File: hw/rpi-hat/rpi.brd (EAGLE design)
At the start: 65 x 56.5 mm, 30 parts, among them U1 BSS138, U2 BSS138, U3 BSS138

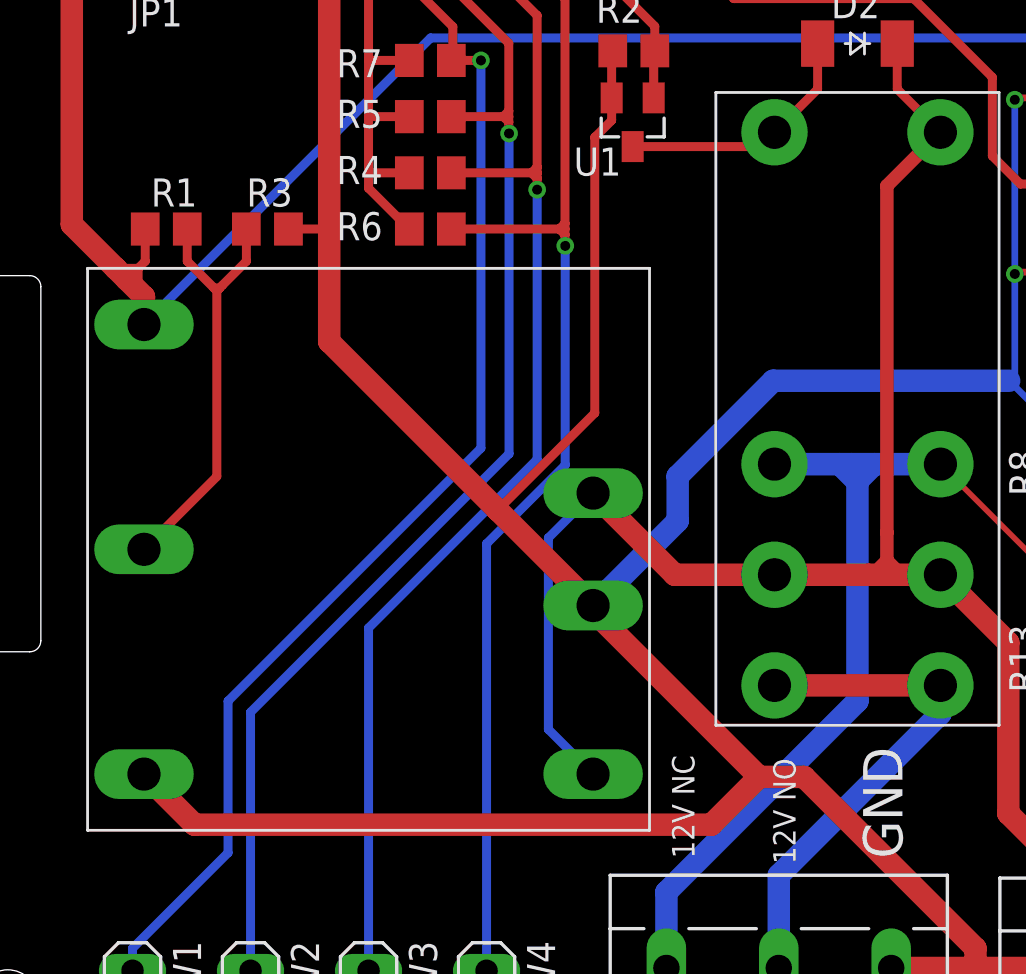
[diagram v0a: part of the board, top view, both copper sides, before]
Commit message: rpi hat: fix a few traces being to close to vias
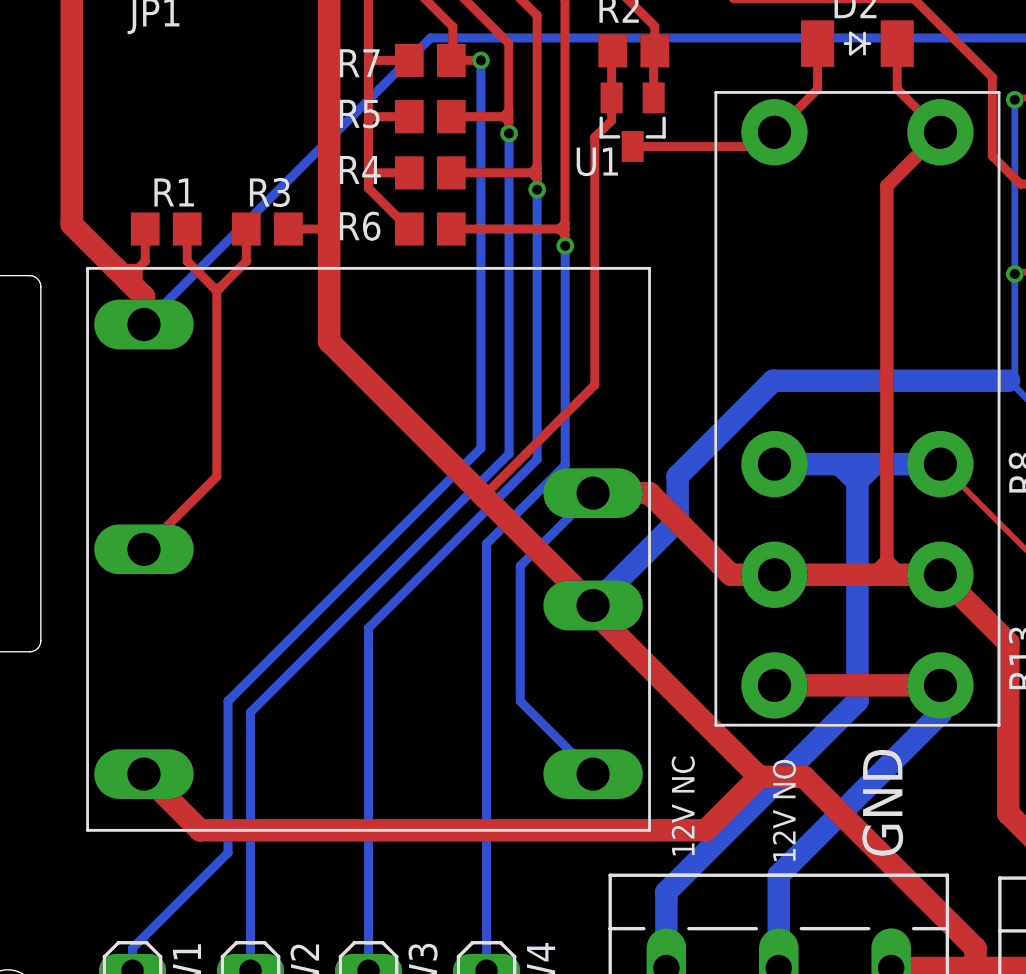
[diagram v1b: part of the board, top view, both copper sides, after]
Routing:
- net +12V: track 81.5 -> 82.5 mm
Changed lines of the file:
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@@
 <wire x1="30.85" y1="46.662" x2="30.8" y2="46.612" width="0.4064" layer="1"/>
 <wire x1="30.8" y1="46.612" x2="30.8" y2="44.534" width="0.4064" layer="1"/>
-<wire x1="9.662" y1="13.97" x2="11.948" y2="11.684" width="1.016" layer="1"/>
-<wire x1="11.948" y1="11.684" x2="35.306" y2="11.684" width="1.016" layer="1"/>
+<wire x1="9.662" y1="13.97" x2="12.202" y2="11.43" width="1.016" layer="1"/>
+<wire x1="12.202" y1="11.43" x2="35.052" y2="11.43" width="1.016" layer="1"/>
 <contactref element="SW4" pad="2"/>
 <contactref element="SW1" pad="2"/>
@@
 <contactref element="SW3" pad="2"/>
 <wire x1="18.034" y1="33.518" x2="18.034" y2="38.608" width="1.016" layer="1"/>
-<wire x1="29.962" y1="21.59" x2="25.649" y2="25.903" width="1.016" layer="1"/>
-<wire x1="25.649" y1="25.903" x2="18.034" y2="33.518" width="1.016" layer="1"/>
+<wire x1="29.962" y1="21.59" x2="25.014" y2="26.538" width="1.016" layer="1"/>
+<wire x1="25.014" y1="26.538" x2="18.034" y2="33.518" width="1.016" layer="1"/>
 <wire x1="16.19" y1="38.608" x2="18.034" y2="38.608" width="0.4064" layer="1"/>
 <wire x1="9.144" y1="2.54" x2="14.478" y2="2.54" width="0.4064" layer="1"/>
@@
 <wire x1="30.8" y1="44.534" x2="30.8" y2="43.518" width="0.4064" layer="1"/>
 <wire x1="30.8" y1="43.518" x2="30.038" y2="42.756" width="0.4064" layer="1"/>
-<wire x1="30.038" y1="42.756" x2="30.038" y2="30.292" width="0.4064" layer="1"/>
-<wire x1="30.038" y1="30.292" x2="25.649" y2="25.903" width="0.4064" layer="1"/>
+<wire x1="30.038" y1="42.756" x2="30.038" y2="31.562" width="0.4064" layer="1"/>
+<wire x1="30.038" y1="31.562" x2="25.014" y2="26.538" width="0.4064" layer="1"/>
 <contactref element="X3" pad="1"/>
 <wire x1="43.434" y1="5.207" x2="47.244" y2="5.207" width="1.016" layer="1"/>
@@
 <wire x1="37.465" y1="13.843" x2="29.962" y2="21.346" width="1.016" layer="1"/>
 <wire x1="29.962" y1="21.59" x2="29.962" y2="21.346" width="1.016" layer="1"/>
-<wire x1="35.306" y1="11.684" x2="37.465" y2="13.843" width="1.016" layer="1"/>
+<wire x1="35.052" y1="11.43" x2="37.465" y2="13.843" width="1.016" layer="1"/>
 <wire x1="39.497" y1="13.843" x2="37.465" y2="13.843" width="1.016" layer="1"/>
 <wire x1="47.244" y1="6.096" x2="39.497" y2="13.843" width="1.016" layer="1"/>
@@
 <contactref element="U$1" pad="P6"/>
 <wire x1="55.84" y1="5.08" x2="48.728" y2="12.192" width="1.016" layer="1"/>
-<wire x1="27.94" y1="24.648" x2="27.94" y2="15.992" width="0.4064" layer="16"/>
-<wire x1="29.962" y1="13.97" x2="27.94" y2="15.992" width="0.4064" layer="16"/>
-<wire x1="29.962" y1="26.67" x2="27.94" y2="24.648" width="0.4064" layer="16"/>
+<wire x1="26.67" y1="23.378" x2="26.67" y2="17.262" width="0.4064" layer="16"/>
+<wire x1="29.962" y1="13.97" x2="26.67" y2="17.262" width="0.4064" layer="16"/>
+<wire x1="29.962" y1="26.67" x2="26.67" y2="23.378" width="0.4064" layer="16"/>
 <wire x1="45.66" y1="42.98" x2="43.71" y2="44.93" width="0.4064" layer="1"/>
 <wire x1="43.71" y1="44.93" x2="43.71" y2="46.99" width="0.4064" layer="1"/>
@@
 <wire x1="38.16" y1="22.98" x2="42.418" y2="22.98" width="1.016" layer="1"/>
 <wire x1="42.418" y1="22.98" x2="43.18" y2="22.98" width="1.016" layer="1"/>
-<wire x1="38.16" y1="22.98" x2="33.652" y2="22.98" width="1.016" layer="1"/>
-<wire x1="33.652" y1="22.98" x2="29.962" y2="26.67" width="1.016" layer="1"/>
+<wire x1="38.16" y1="22.98" x2="36.192" y2="22.98" width="1.016" layer="1"/>
+<wire x1="36.192" y1="22.98" x2="32.502" y2="26.67" width="1.016" layer="1"/>
+<wire x1="32.502" y1="26.67" x2="29.962" y2="26.67" width="1.016" layer="1"/>
 <wire x1="43.24" y1="23.04" x2="43.18" y2="22.98" width="0.6096" layer="1"/>
-<wire x1="43.24" y1="40.56" x2="43.24" y2="24.892" width="0.6096" layer="1"/>
-<wire x1="43.24" y1="24.892" x2="43.24" y2="23.622" width="0.6096" layer="1"/>
+<wire x1="43.24" y1="40.56" x2="43.24" y2="23.622" width="0.6096" layer="1"/>
 <wire x1="43.24" y1="23.622" x2="43.24" y2="23.04" width="0.6096" layer="1"/>
 <wire x1="42.598" y1="22.98" x2="43.24" y2="23.622" width="0.6096" layer="1"/>

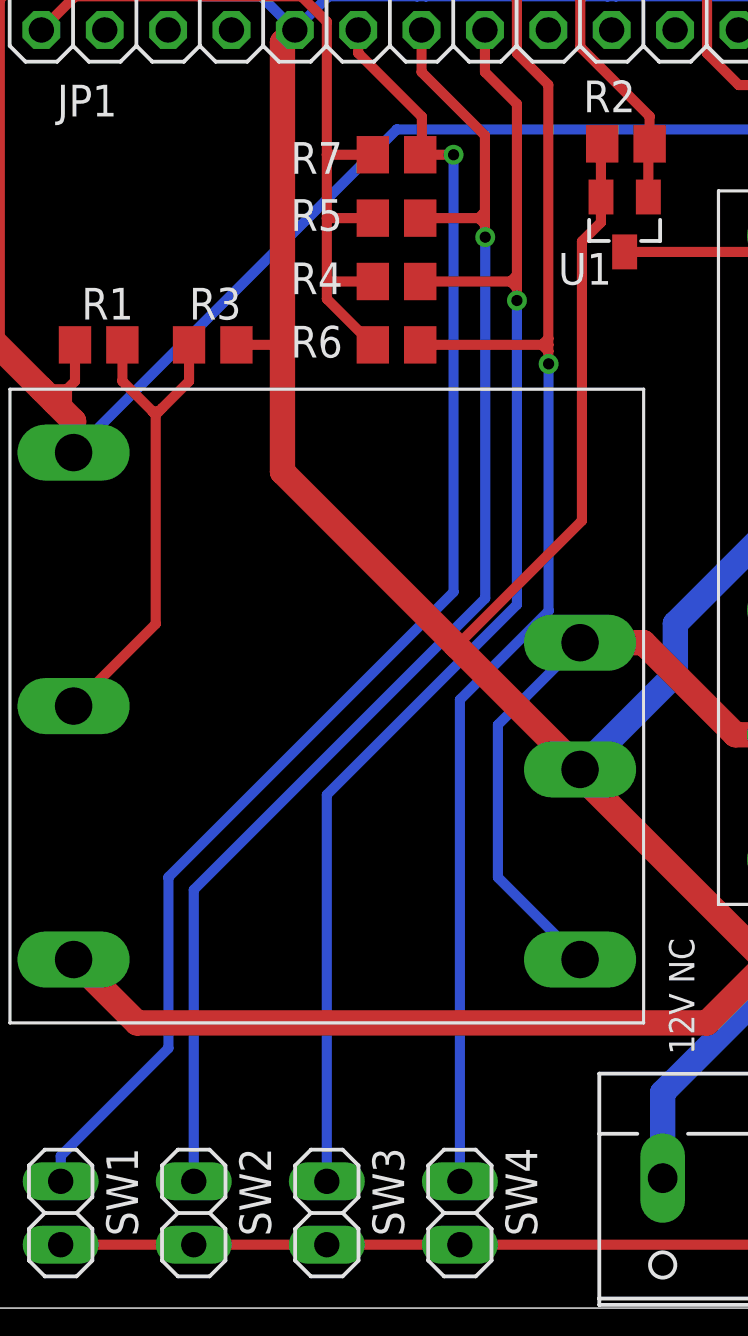
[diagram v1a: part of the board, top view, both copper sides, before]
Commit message: rpi hat: fix more traces being to close to vias
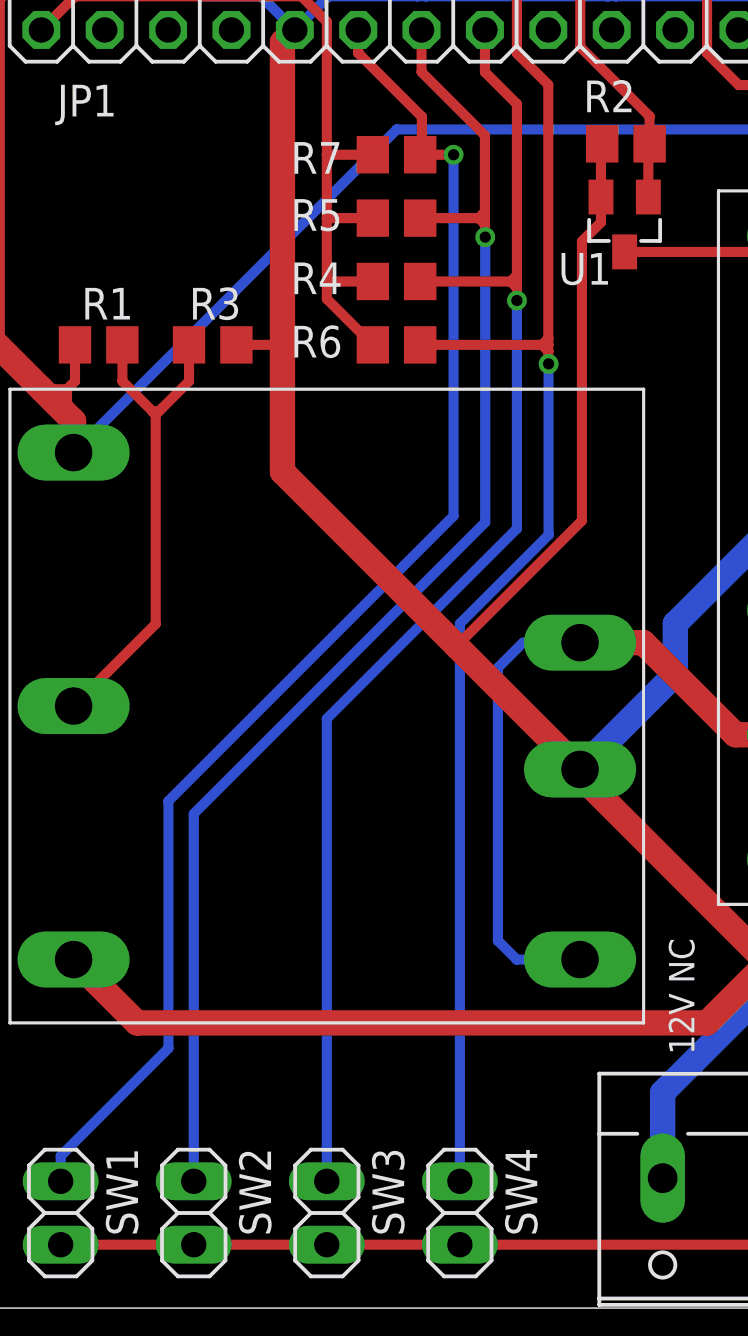
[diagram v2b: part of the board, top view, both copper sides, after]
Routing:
- net +12V: track 82.5 -> 85.4 mm
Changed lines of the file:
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@@
 <contactref element="U$1" pad="P6"/>
 <wire x1="55.84" y1="5.08" x2="48.728" y2="12.192" width="1.016" layer="1"/>
-<wire x1="26.67" y1="23.378" x2="26.67" y2="17.262" width="0.4064" layer="16"/>
-<wire x1="29.962" y1="13.97" x2="26.67" y2="17.262" width="0.4064" layer="16"/>
-<wire x1="29.962" y1="26.67" x2="26.67" y2="23.378" width="0.4064" layer="16"/>
+<wire x1="26.67" y1="25.664" x2="26.67" y2="14.722" width="0.4064" layer="16"/>
+<wire x1="29.962" y1="13.97" x2="27.422" y2="13.97" width="0.4064" layer="16"/>
+<wire x1="27.422" y1="13.97" x2="26.67" y2="14.722" width="0.4064" layer="16"/>
+<wire x1="29.962" y1="26.67" x2="27.676" y2="26.67" width="0.4064" layer="16"/>
+<wire x1="27.676" y1="26.67" x2="26.67" y2="25.664" width="0.4064" layer="16"/>
 <wire x1="45.66" y1="42.98" x2="43.71" y2="44.93" width="0.4064" layer="1"/>
 <wire x1="43.71" y1="44.93" x2="43.71" y2="46.99" width="0.4064" layer="1"/>
@@
 <via x="27.432" y="40.386" extent="1-16" drill="0.45" diameter="0.8"/>
 <wire x1="27.432" y1="40.894" x2="27.432" y2="40.386" width="0.4064" layer="1"/>
-<wire x1="27.432" y1="40.386" x2="27.432" y2="28.194" width="0.4064" layer="16"/>
-<wire x1="27.432" y1="28.194" x2="19.812" y2="20.574" width="0.4064" layer="16"/>
-<wire x1="19.812" y1="5.08" x2="19.812" y2="20.574" width="0.4064" layer="16"/>
+<wire x1="27.432" y1="40.386" x2="27.432" y2="31.242" width="0.4064" layer="16"/>
+<wire x1="27.432" y1="31.242" x2="19.812" y2="23.622" width="0.4064" layer="16"/>
+<wire x1="19.812" y1="5.08" x2="19.812" y2="23.622" width="0.4064" layer="16"/>
 <wire x1="27.178" y1="41.148" x2="27.432" y2="41.402" width="0.4064" layer="1"/>
 <wire x1="27.178" y1="41.148" x2="27.432" y2="40.894" width="0.4064" layer="1"/>
@@
 <wire x1="28.69" y1="37.858" x2="28.702" y2="37.846" width="0.4064" layer="1"/>
 <via x="28.702" y="37.846" extent="1-16" drill="0.45" diameter="0.8"/>
-<wire x1="28.702" y1="37.846" x2="28.702" y2="27.94" width="0.4064" layer="16"/>
-<wire x1="25.146" y1="24.384" x2="28.702" y2="27.94" width="0.4064" layer="16"/>
-<wire x1="25.146" y1="5.08" x2="25.146" y2="24.384" width="0.4064" layer="16"/>
+<wire x1="28.702" y1="37.846" x2="28.702" y2="30.988" width="0.4064" layer="16"/>
+<wire x1="25.146" y1="27.432" x2="28.702" y2="30.988" width="0.4064" layer="16"/>
+<wire x1="25.146" y1="5.08" x2="25.146" y2="27.432" width="0.4064" layer="16"/>
 <wire x1="28.436" y1="38.608" x2="28.69" y2="38.862" width="0.4064" layer="1"/>
 <wire x1="28.436" y1="38.608" x2="28.69" y2="38.354" width="0.4064" layer="1"/>
@@
 <wire x1="23.556" y1="46.228" x2="24.892" y2="46.228" width="0.4064" layer="1"/>
 <via x="24.892" y="46.228" extent="1-16" drill="0.45" diameter="0.8"/>
-<wire x1="24.892" y1="46.228" x2="24.892" y2="28.702" width="0.4064" layer="16"/>
-<wire x1="13.462" y1="17.272" x2="13.462" y2="10.414" width="0.4064" layer="16"/>
+<wire x1="24.892" y1="46.228" x2="24.892" y2="31.75" width="0.4064" layer="16"/>
+<wire x1="13.462" y1="20.32" x2="13.462" y2="10.414" width="0.4064" layer="16"/>
 <wire x1="9.144" y1="6.096" x2="13.462" y2="10.414" width="0.4064" layer="16"/>
-<wire x1="24.892" y1="28.702" x2="13.462" y2="17.272" width="0.4064" layer="16"/>
+<wire x1="24.892" y1="31.75" x2="13.462" y2="20.32" width="0.4064" layer="16"/>
 <wire x1="9.144" y1="5.08" x2="9.144" y2="6.096" width="0.4064" layer="16"/>
 <wire x1="21.07" y1="51.23" x2="21.07" y2="50.304" width="0.4064" layer="1"/>
@@
 <wire x1="26.15" y1="42.938" x2="26.162" y2="42.926" width="0.4064" layer="1"/>
 <via x="26.162" y="42.926" extent="1-16" drill="0.45" diameter="0.8"/>
-<wire x1="26.162" y1="42.926" x2="26.162" y2="28.448" width="0.4064" layer="16"/>
-<wire x1="26.162" y1="28.448" x2="14.478" y2="16.764" width="0.4064" layer="16"/>
-<wire x1="14.478" y1="5.08" x2="14.478" y2="16.764" width="0.4064" layer="16"/>
+<wire x1="26.162" y1="42.926" x2="26.162" y2="31.496" width="0.4064" layer="16"/>
+<wire x1="26.162" y1="31.496" x2="14.478" y2="19.812" width="0.4064" layer="16"/>
+<wire x1="14.478" y1="5.08" x2="14.478" y2="19.812" width="0.4064" layer="16"/>
 <wire x1="25.908" y1="43.688" x2="25.908" y2="43.7" width="0.4064" layer="1"/>
 <wire x1="25.908" y1="43.7" x2="26.15" y2="43.942" width="0.4064" layer="1"/>
